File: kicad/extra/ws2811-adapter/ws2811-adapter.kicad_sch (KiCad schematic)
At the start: 5 parts, among them J1 Conn_01x03_Pin, J2 RJ45 P1, J3 RJ45 P2, J4 RJ45 P3, J5 Conn_01x03_Socket

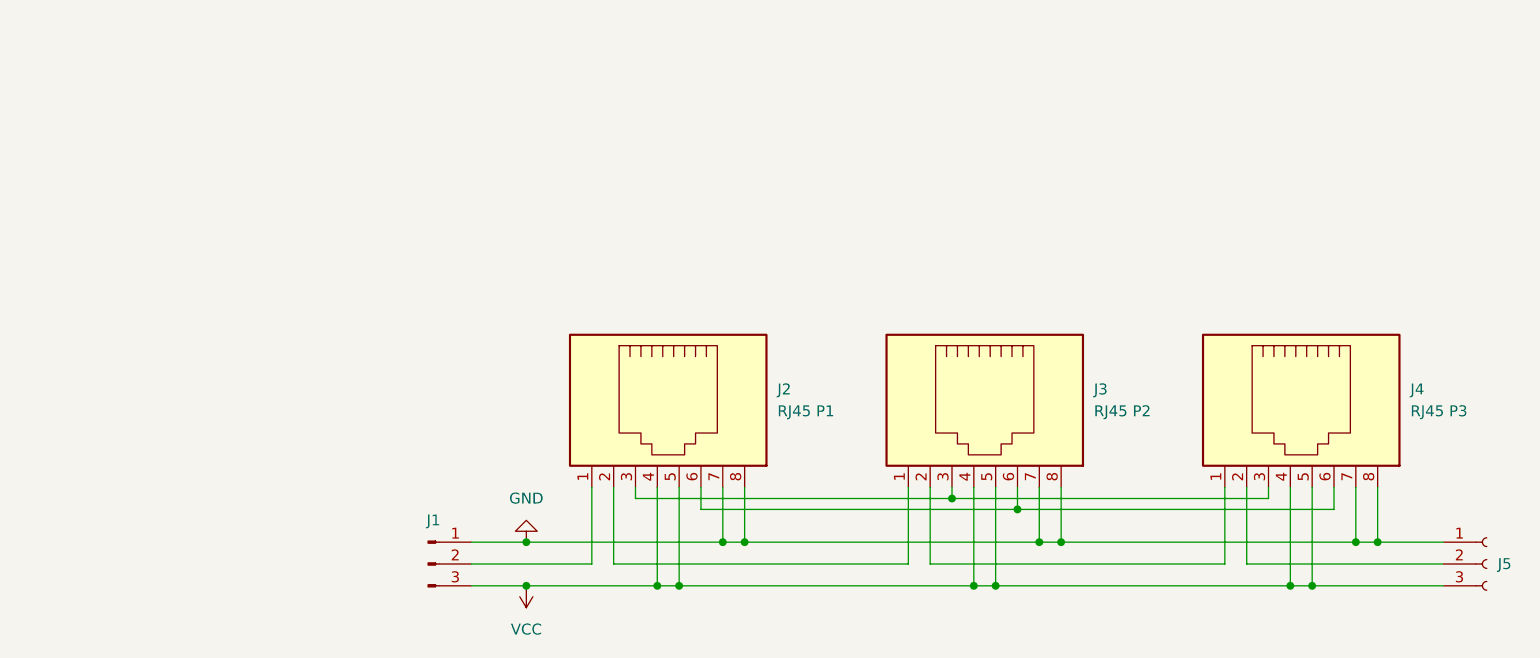
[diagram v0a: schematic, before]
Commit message: feat: Rework WS2811 boards (Rev 2.0)
* Change RJ45 pinout: The data signal is always paired with a ground
  line to increase signal stability, and the changed wireing eases the
  traces on the boards.

* All WS2811 driver boards have a three pin header for direct drive now.
  They can be directly connected to a signal decoder, e.g. for testing.

* The adapter boards has jumper pins to bypass RJ45 jacks, in case you
  want to connect another board using the final pin header.

* Change pin header component to a better available JCSC parts number.

* Move RJ45 jacks on driver boards a bit more off the board, so that
  there is less space between the jack and the outer side of the Watti
  carrier. This makes it easier to plug in and out RJ45 cables as
  the latches are easier to reach.

Fixes #4
Fixes #5
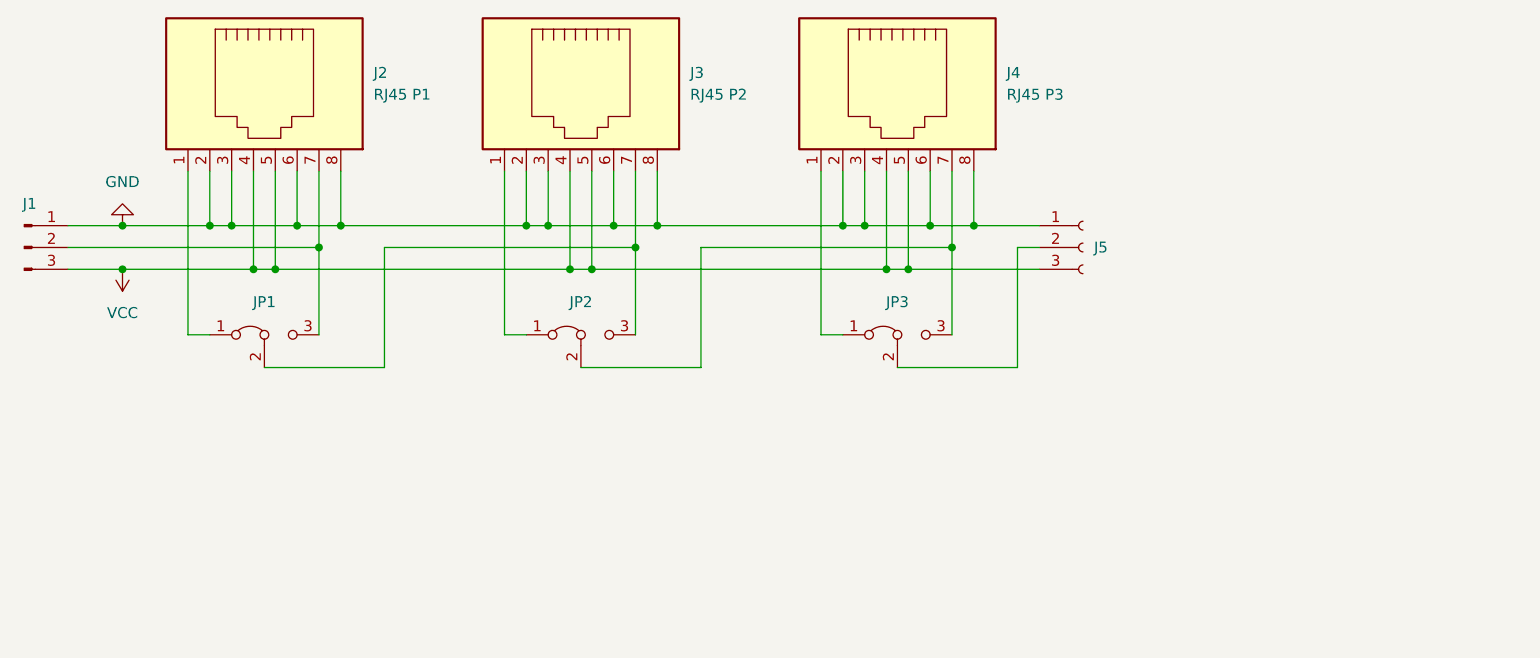
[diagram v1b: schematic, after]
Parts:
- added JP1, JP2, JP3: Jumper_3_Bridged12, Connector_PinHeader_2.54mm:PinHeader_1x03_P2.54mm_Vertical, symbol Jumper:Jumper_3_Bridged12
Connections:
- net GND: now also J2.2, J2.3, J2.6, J3.2, J3.3, J3.6, J4.2, J4.3, J4.6; no longer J2.7, J3.7, J4.7
- net at J2.1: now also JP1.1 (A); no longer J1.2 (Pin_2)
- net at J3.1: now also JP2.1 (A); no longer J2.2
- net at J5.2 (Pin_2): now also JP3.2 (C); no longer J4.2
- net at J4.1: now also JP3.1 (A); no longer J3.2
- new net: J4.7, JP2.2 (C), JP3.3 (B)
- new net: J3.7, JP1.2 (C), JP2.3 (B)
- new net: J1.2 (Pin_2), J2.7, JP1.3 (B)
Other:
- moved on the sheet: J1, J2, J3, J4, J5
